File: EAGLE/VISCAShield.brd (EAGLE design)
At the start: 54.3 x 59.7 mm, 35 parts, among them J1 RJHSE-5381

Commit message: Some revisions.
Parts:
- added C1, C2, C3, C4, C5: 1.0uF, SparkFun-Capacitors:0805
- added U1: MAX3232, SparkFun-IC-Comms:SO16
- moved 12V 14.5 mm to (25.4, 47.0), turned to 90 degrees
- moved J1 4.02 mm to (27.9, 61.0)
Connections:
- new net 232RX: J1.6, U1.13
- new net 232TX: J1.3, U1.14
- new net C1+: C1.1, U1.1
- new net C1-: C1.2, U1.3
- new net C2+: C2.1, U1.4
- new net C2-: C2.2, U1.5
- new net RS232V+: C3.1, U1.2
- new net RS232V-: C4.1, U1.6
- net 5V: now also C5.1, U1.16
- net GND: now also C3.2, C4.2, C5.2, U1.10, U1.15, U1.8
- net RX: now also U1.12; no longer J1.6
- net TX: now also U1.11; no longer J1.3
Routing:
- net 232TX: track 0.00 -> 25.6 mm, vias 0 -> 1
- net 232RX: track 0.00 -> 23.0 mm, vias 0 -> 1
- net 5V: track 211.8 -> 230.2 mm, vias 0 -> 1
- net RX: track 28.1 -> 9.95 mm
- net TX: track 27.8 -> 14.5 mm
- net RS232V-: track 0.00 -> 8.52 mm
- net RS232V+: track 0.00 -> 6.50 mm
- net C2-: track 0.00 -> 2.92 mm
- net C1+: track 0.00 -> 2.70 mm
- net C2+: track 0.00 -> 2.70 mm
- net C1-: track 0.00 -> 2.39 mm
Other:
- board size 54.3 x 59.7 mm -> 54.3 x 63.5 mm

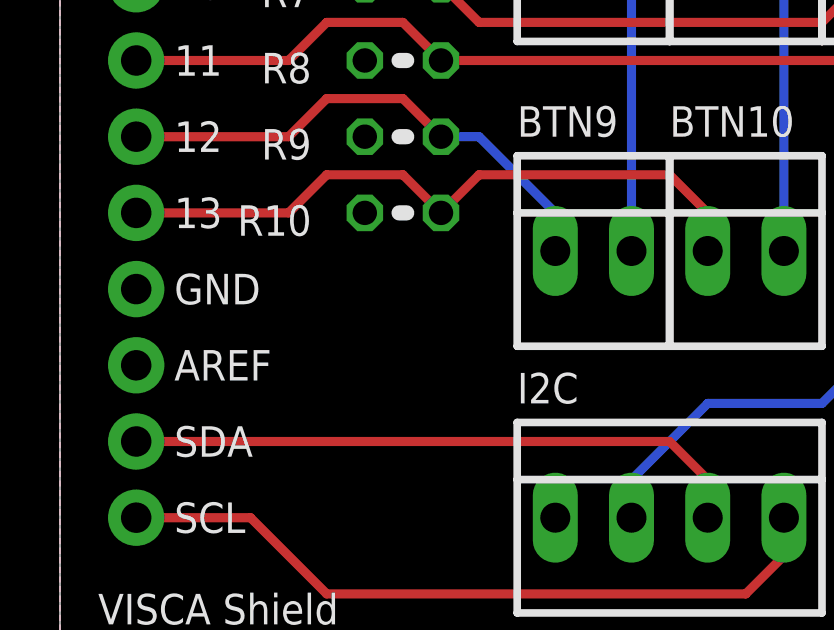
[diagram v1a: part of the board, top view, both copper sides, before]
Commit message: Add optional AREF input jumper.  Clean up unused nets from schematic.
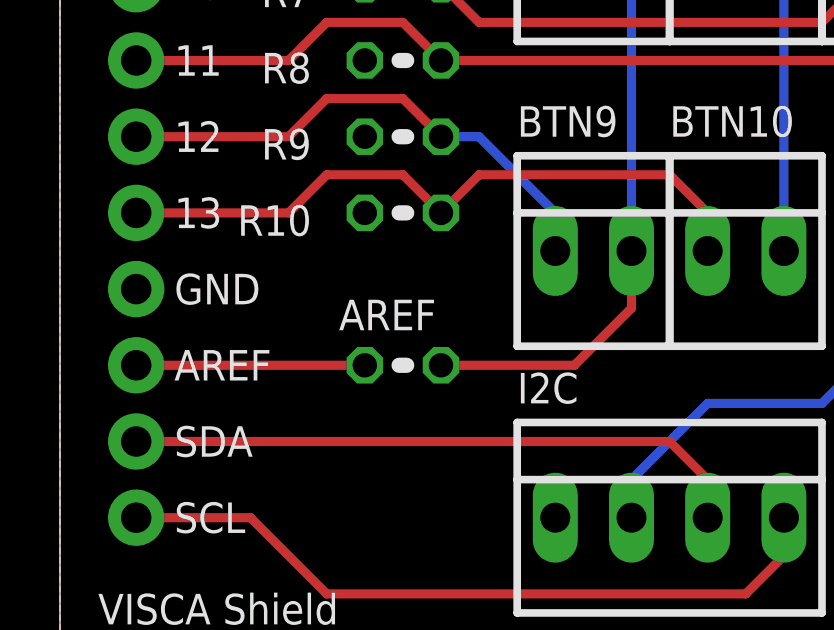
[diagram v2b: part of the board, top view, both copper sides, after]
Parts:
- added AREF: 0ohm, BeagleBone_Black_Wireless:0204V
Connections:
- new net AREF: AREF.1, B1.AREF
- net 5V: now also AREF.2
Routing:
- net 5V: track 230.2 -> 239.2 mm
- net AREF: track 0.00 -> 7.62 mm
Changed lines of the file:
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@@
 <drawing>
 <settings>
-<setting alwaysvectorfont="yes"/>
+<setting alwaysvectorfont="no"/>
 <setting verticaltext="up"/>
 </settings>
@@
 <attribute name="VALUE" x="8.89" y="47.879" size="0.6096" layer="27" font="vector" ratio="20" rot="R270" align="top-center" display="off"/>
 </element>
+<element name="AREF" library="BeagleBone_Black_Wireless" library_urn="urn:adsk.eagle:library:6644236" package="0204V" package3d_urn="urn:adsk.eagle:package:8118463/1" value="0ohm" x="11.43" y="15.24" smashed="yes">
+<attribute name="NAME" x="9.2964" y="16.4084" size="1.016" layer="25" ratio="12"/>
+<attribute name="VALUE" x="9.2964" y="12.9286" size="1.27" layer="27" ratio="12" display="off"/>
+</element>
 </elements>
 <signals>
@@
 <wire x1="15.24" y1="46.99" x2="19.05" y2="43.18" width="0.3048" layer="16"/>
 <wire x1="19.05" y1="43.18" x2="19.05" y2="39.37" width="0.3048" layer="16"/>
+<contactref element="AREF" pad="2"/>
+<wire x1="12.7" y1="15.24" x2="17.145" y2="15.24" width="0.3048" layer="1"/>
+<wire x1="17.145" y1="15.24" x2="19.05" y2="17.145" width="0.3048" layer="1"/>
+<wire x1="19.05" y1="17.145" x2="19.05" y2="19.05" width="0.3048" layer="1"/>
 </signal>
 <signal name="PAN">
@@
 <wire x1="28.575" y1="53.975" x2="29.47" y2="54.87" width="0.3048" layer="16"/>
 </signal>
+<signal name="AREF">
+<contactref element="B1" pad="AREF"/>
+<contactref element="AREF" pad="1"/>
+<wire x1="2.54" y1="15.24" x2="10.16" y2="15.24" width="0.3048" layer="1"/>
+</signal>
 </signals>

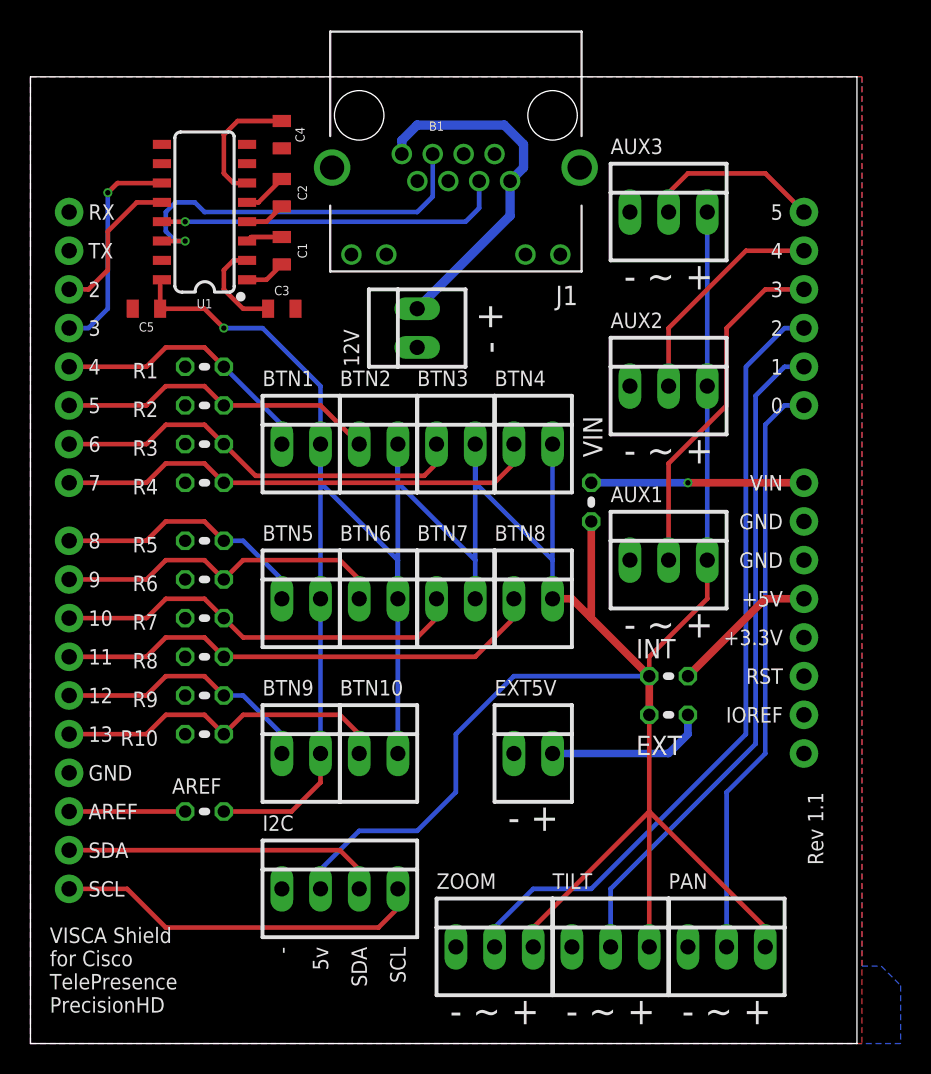
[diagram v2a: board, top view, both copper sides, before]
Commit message: Successful build of Visca shield & more testing of control code.
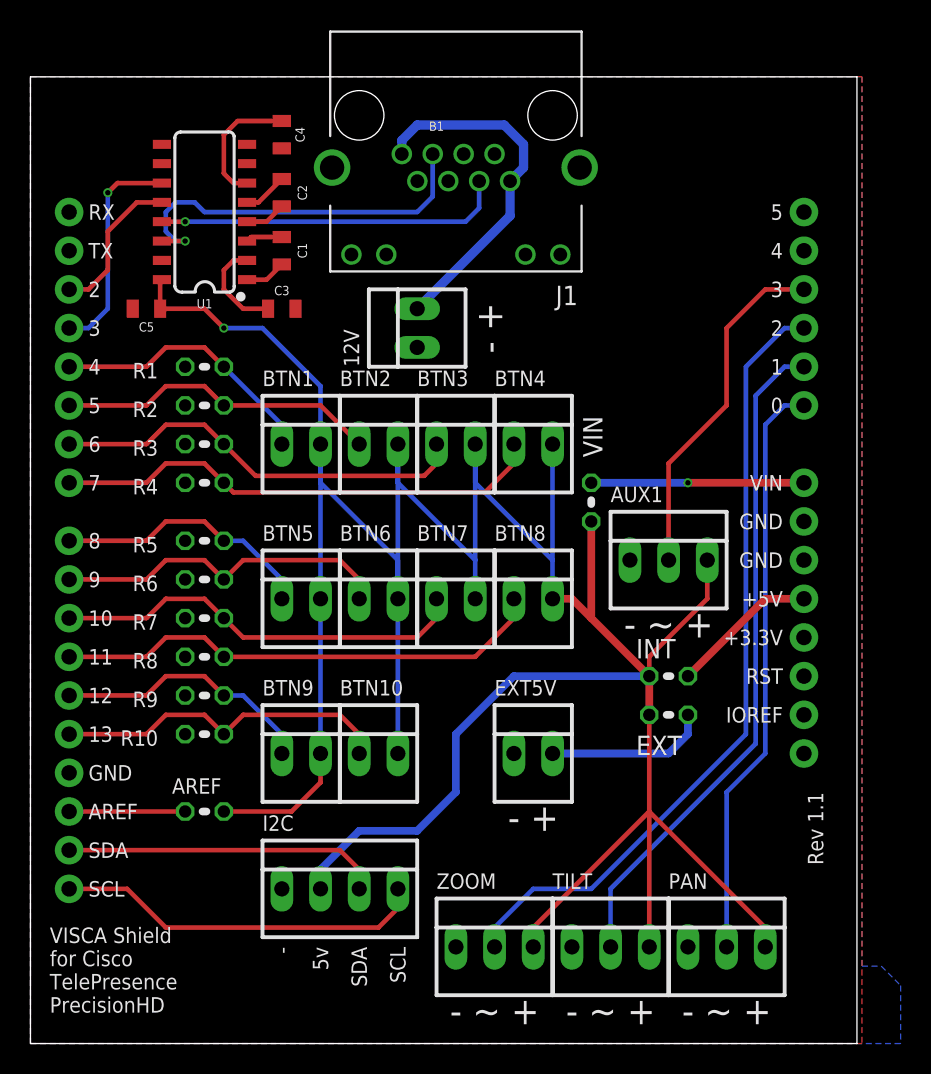
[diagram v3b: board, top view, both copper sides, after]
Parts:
- removed AUX2, AUX3: 22-23-2031, con-molex:22-23-2031
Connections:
- removed net AUX2: AUX2.2, B1.A4
- removed net AUX3: AUX3.2, B1.A5
- net 5V: no longer AUX2.3, AUX3.3
- net GND: no longer AUX2.1, AUX3.1
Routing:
- net 5V: track 239.2 -> 216.3 mm
- net AUX2: track 14.8 -> 0.00 mm
- net AUX3: track 11.7 -> 0.00 mm
- net B4: track 32.1 -> 32.6 mm
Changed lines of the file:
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@@
 <?xml version="1.0" encoding="utf-8"?>
 <!DOCTYPE eagle SYSTEM "eagle.dtd">
-<eagle version="9.4.2">
+<eagle version="9.6.2">
 <drawing>
 <settings>
@@
 PrecisionHD</text>
 <text x="52.07" y="16.51" size="1.016" layer="25" rot="R270" align="top-left">Rev 1.1</text>
-<text x="41.91" y="49.53" size="1.778" layer="25" align="bottom-center">- ~ +</text>
-<text x="41.91" y="38.1" size="1.778" layer="25" align="bottom-center">- ~ +</text>
 <text x="41.91" y="26.67" size="1.778" layer="25" align="bottom-center">- ~ +</text>
 <text x="45.72" y="1.27" size="1.778" layer="25" align="bottom-center">- ~ +</text>
@@
 <attribute name="VALUE" x="38.1" y="26.67" size="1.016" layer="27" ratio="10" display="off"/>
 </element>
-<element name="AUX2" library="con-molex" library_urn="urn:adsk.eagle:library:165" package="22-23-2031" package3d_urn="urn:adsk.eagle:package:8078634/1" value="22-23-2031" x="41.91" y="43.18" smashed="yes">
-<attribute name="MF" value="MOLEX" x="41.91" y="43.18" size="1.778" layer="27" display="off"/>
-<attribute name="MPN" value="22-23-2031" x="41.91" y="43.18" size="1.778" layer="27" display="off"/>
-<attribute name="NAME" x="38.1" y="46.99" size="1.016" layer="25" ratio="10"/>
-<attribute name="OC_FARNELL" value="1462950" x="41.91" y="43.18" size="1.778" layer="27" display="off"/>
-<attribute name="OC_NEWARK" value="30C0862" x="41.91" y="43.18" size="1.778" layer="27" display="off"/>
-<attribute name="POPULARITY" value="35" x="41.91" y="43.18" size="1.778" layer="27" display="off"/>
-<attribute name="VALUE" x="38.1" y="38.1" size="1.016" layer="27" ratio="10" display="off"/>
-</element>
-<element name="AUX3" library="con-molex" library_urn="urn:adsk.eagle:library:165" package="22-23-2031" package3d_urn="urn:adsk.eagle:package:8078634/1" value="22-23-2031" x="41.91" y="54.61" smashed="yes">
-<attribute name="MF" value="MOLEX" x="41.91" y="54.61" size="1.778" layer="27" display="off"/>
-<attribute name="MPN" value="22-23-2031" x="41.91" y="54.61" size="1.778" layer="27" display="off"/>
-<attribute name="NAME" x="38.1" y="58.42" size="1.016" layer="25" ratio="10"/>
-<attribute name="OC_FARNELL" value="1462950" x="41.91" y="54.61" size="1.778" layer="27" display="off"/>
-<attribute name="OC_NEWARK" value="30C0862" x="41.91" y="54.61" size="1.778" layer="27" display="off"/>
-<attribute name="POPULARITY" value="35" x="41.91" y="54.61" size="1.778" layer="27" display="off"/>
-<attribute name="VALUE" x="38.1" y="49.53" size="1.016" layer="27" ratio="10" display="off"/>
-</element>
 <element name="I2C" library="con-molex" library_urn="urn:adsk.eagle:library:165" package="22-23-2041" package3d_urn="urn:adsk.eagle:package:8078635/1" value="22-23-2041" x="20.32" y="10.16" smashed="yes">
 <attribute name="MF" value="MOLEX" x="20.32" y="10.16" size="1.778" layer="27" display="off"/>
@@
 <contactref element="ZOOM" pad="1"/>
 <contactref element="AUX1" pad="1"/>
-<contactref element="AUX2" pad="1"/>
-<contactref element="AUX3" pad="1"/>
 <contactref element="EXT5V" pad="1"/>
 <contactref element="I2C" pad="1"/>
@@
 <contactref element="U1" pad="10"/>
 <contactref element="U1" pad="8"/>
+<wire x1="25.41" y1="56.64" x2="30.48" y2="58.42" width="0" layer="19" extent="1-1"/>
+<wire x1="16.51" y1="58.79" x2="25.41" y2="56.64" width="0" layer="19" extent="1-1"/>
+<wire x1="14.23" y1="59.055" x2="16.51" y2="58.79" width="0" layer="19" extent="1-1"/>
+<wire x1="8.63" y1="57.785" x2="14.23" y2="59.055" width="0" layer="19" extent="1-1"/>
+<wire x1="8.63" y1="51.435" x2="8.63" y2="57.785" width="0" layer="19" extent="1-1"/>
+<wire x1="6.72" y1="48.26" x2="8.63" y2="51.435" width="0" layer="19" extent="1-1"/>
+<wire x1="10.16" y1="44.45" x2="6.72" y2="48.26" width="0" layer="19" extent="1-1"/>
+<wire x1="10.16" y1="41.91" x2="10.16" y2="44.45" width="0" layer="19" extent="1-1"/>
+<wire x1="10.16" y1="39.37" x2="10.16" y2="41.91" width="0" layer="19" extent="1-1"/>
+<wire x1="10.16" y1="36.83" x2="10.16" y2="39.37" width="0" layer="19" extent="1-1"/>
+<wire x1="10.16" y1="33.02" x2="10.16" y2="36.83" width="0" layer="19" extent="1-1"/>
+<wire x1="10.16" y1="30.48" x2="10.16" y2="33.02" width="0" layer="19" extent="1-1"/>
+<wire x1="10.16" y1="27.94" x2="10.16" y2="30.48" width="0" layer="19" extent="1-1"/>
+<wire x1="10.16" y1="25.4" x2="10.16" y2="27.94" width="0" layer="19" extent="1-1"/>
+<wire x1="10.16" y1="22.86" x2="10.16" y2="25.4" width="0" layer="19" extent="1-1"/>
+<wire x1="10.16" y1="20.32" x2="10.16" y2="22.86" width="0" layer="19" extent="1-1"/>
+<wire x1="2.54" y1="17.78" x2="10.16" y2="20.32" width="0" layer="19" extent="1-1"/>
+<wire x1="17.41" y1="48.26" x2="10.16" y2="44.45" width="0" layer="19" extent="1-1"/>
+<wire x1="25.4" y1="45.72" x2="17.41" y2="48.26" width="0" layer="19" extent="1-1"/>
+<wire x1="16.51" y1="10.16" x2="10.16" y2="20.32" width="0" layer="19" extent="1-1"/>
+<wire x1="27.94" y1="6.35" x2="16.51" y2="10.16" width="0" layer="19" extent="1-1"/>
+<wire x1="35.56" y1="6.35" x2="27.94" y2="6.35" width="0" layer="19" extent="1-1"/>
+<wire x1="43.18" y1="6.35" x2="35.56" y2="6.35" width="0" layer="19" extent="1-1"/>
+<wire x1="31.75" y1="19.05" x2="27.94" y2="6.35" width="0" layer="19" extent="1-1"/>
+<wire x1="39.37" y1="31.75" x2="31.75" y2="19.05" width="0" layer="19" extent="1-1"/>
+<wire x1="50.8" y1="31.75" x2="39.37" y2="31.75" width="0" layer="19" extent="1-1"/>
+<wire x1="50.8" y1="34.29" x2="50.8" y2="31.75" width="0" layer="19" extent="1-1"/>
 </signal>
 <signal name="5V">
@@
 <wire x1="34.29" y1="31.75" x2="34.29" y2="29.21" width="0.3048" layer="16"/>
 <contactref element="AUX1" pad="3"/>
-<contactref element="AUX2" pad="3"/>
-<contactref element="AUX3" pad="3"/>
-<wire x1="44.45" y1="54.61" x2="44.45" y2="43.18" width="0.3048" layer="16"/>
-<wire x1="44.45" y1="43.18" x2="44.45" y2="31.75" width="0.3048" layer="16"/>
 <contactref element="I2C" pad="2"/>
 <contactref element="INT" pad="1"/>
@@
 <wire x1="33.02" y1="6.35" x2="33.02" y2="7.62" width="0.3048" layer="1"/>
 <wire x1="33.02" y1="7.62" x2="40.64" y2="15.24" width="0.3048" layer="1"/>
-<wire x1="19.05" y1="10.16" x2="19.05" y2="11.43" width="0.3048" layer="16"/>
-<wire x1="19.05" y1="11.43" x2="21.59" y2="13.97" width="0.3048" layer="16"/>
-<wire x1="21.59" y1="13.97" x2="25.4" y2="13.97" width="0.3048" layer="16"/>
-<wire x1="25.4" y1="13.97" x2="27.94" y2="16.51" width="0.3048" layer="16"/>
-<wire x1="27.94" y1="16.51" x2="27.94" y2="20.32" width="0.3048" layer="16"/>
-<wire x1="27.94" y1="20.32" x2="31.75" y2="24.13" width="0.3048" layer="16"/>
-<wire x1="31.75" y1="24.13" x2="40.64" y2="24.13" width="0.3048" layer="16"/>
+<wire x1="19.05" y1="10.16" x2="19.05" y2="11.43" width="0.508" layer="16"/>
+<wire x1="19.05" y1="11.43" x2="21.59" y2="13.97" width="0.508" layer="16"/>
+<wire x1="21.59" y1="13.97" x2="25.4" y2="13.97" width="0.508" layer="16"/>
+<wire x1="25.4" y1="13.97" x2="27.94" y2="16.51" width="0.508" layer="16"/>
+<wire x1="27.94" y1="16.51" x2="27.94" y2="20.32" width="0.508" layer="16"/>
+<wire x1="27.94" y1="20.32" x2="31.75" y2="24.13" width="0.508" layer="16"/>
+<wire x1="31.75" y1="24.13" x2="40.64" y2="24.13" width="0.508" layer="16"/>
 <contactref element="VIN" pad="1"/>
 <wire x1="40.64" y1="21.59" x2="40.64" y2="24.13" width="0.508" layer="1"/>
@@
 <wire x1="8.89" y1="38.1" x2="7.62" y2="36.83" width="0.3048" layer="1"/>
 <wire x1="7.62" y1="36.83" x2="2.54" y2="36.83" width="0.3048" layer="1"/>
-<wire x1="12.7" y1="36.83" x2="30.48" y2="36.83" width="0.3048" layer="1"/>
-<wire x1="30.48" y1="36.83" x2="31.75" y2="38.1" width="0.3048" layer="1"/>
+<wire x1="12.7" y1="36.83" x2="13.335" y2="36.195" width="0.3048" layer="1"/>
+<wire x1="29.845" y1="36.195" x2="13.335" y2="36.195" width="0.3048" layer="1"/>
+<wire x1="29.845" y1="36.195" x2="31.75" y2="38.1" width="0.3048" layer="1"/>
 <wire x1="31.75" y1="38.1" x2="31.75" y2="39.37" width="0.3048" layer="1"/>
 </signal>
@@
 <wire x1="48.26" y1="49.53" x2="50.8" y2="49.53" width="0.3048" layer="1"/>
 </signal>
-<signal name="AUX2">
-<contactref element="B1" pad="A4"/>
-<contactref element="AUX2" pad="2"/>
-<wire x1="41.91" y1="43.18" x2="41.91" y2="46.99" width="0.3048" layer="1"/>
-<wire x1="41.91" y1="46.99" x2="46.99" y2="52.07" width="0.3048" layer="1"/>
-<wire x1="46.99" y1="52.07" x2="50.8" y2="52.07" width="0.3048" layer="1"/>
-</signal>
-<signal name="AUX3">
-<contactref element="B1" pad="A5"/>
-<contactref element="AUX3" pad="2"/>
-<wire x1="41.91" y1="54.61" x2="41.91" y2="55.88" width="0.3048" layer="1"/>
-<wire x1="41.91" y1="55.88" x2="43.18" y2="57.15" width="0.3048" layer="1"/>
-<wire x1="48.26" y1="57.15" x2="50.8" y2="54.61" width="0.3048" layer="1"/>
-<wire x1="43.18" y1="57.15" x2="48.26" y2="57.15" width="0.3048" layer="1"/>
-</signal>
 <signal name="EXT5V">
